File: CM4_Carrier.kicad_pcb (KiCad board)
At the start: 4 copper layers, 47 x 88.8 mm, 102 parts, among them J1 Conn_01x22_Female, J10 Conn_01x20, J12 10018783-11200TLF, J13 BM04B-GHS-TBT(LF)(SN)(N), J14 BM04B-GHS-TBT(LF)(SN)(N), J15 Conn_01x22_Female, J16 XT30, J17 Molex 470531000, J18 BM04B-GHS-TBT(LF)(SN)(N), J2 Conn_01x22_Female, J21 BM04B-GHS-TBT(LF)(SN)(N), J3 USB4085-GF-A_REVA, J4 2199119-4, J6 THD-02-R, J7 Micro_SD_Card_Det, J8 HDMI_D_1.4, J9 Conn_02x08_Odd_Even, Q1 DMP3013SFV-7, SW1 SW_SPST, U1 TPD4EUSB30, U10 AP22653W6, U11 EMC2301-1-ACZL-TR, U12 RT9742SNGV, U13 FSUSB42MUX, U18 RT9742GGJ5, U2 TPD4EUSB30, U3 LMR33640DDDAR, U4 TPD4EUSB30, U6 USB2514B-I/M2, U7 AP22653W6, U9 74LVC1G07SE-7, Y1 ECS-240-18-33-JGN-TR

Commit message: lots of changes, added usb power connections, gpio, hdmi, etc
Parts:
- removed J12: 10018783-11200TLF, CM4IO:PCIex1-36
- removed J4: 2199119-4, Open-HD:TE_2199119-4
- removed J6: THD-02-R, Connector_PinHeader_2.54mm:PinHeader_2x02_P2.54mm_Vertical
- removed R5: 0R, Resistor_SMD:R_0805_2012Metric_Pad1.15x1.40mm_HandSolder
- added TP1: TestPoint, Connector_PinHeader_2.00mm:PinHeader_1x01_P2.00mm_Vertical, F.Cu at (175.1, 80.8)
- R2, R3: moved to F.Cu
- R6, R7: moved to B.Cu
- moved R7 168.1 mm to (128.7, 88.5), turned to -90 degrees
- moved R6 165.6 mm to (126.1, 87.0), turned to 90 degrees
- moved U1 15.0 mm to (153.9, 101.9), turned to 90 degrees
- moved D1 13.7 mm to (94.0, 115.3)
- moved D2 13.7 mm to (85.2, 115.3)
- moved R1 13.7 mm to (88.2, 115.3)
- moved R10 13.7 mm to (97.0, 115.3)
- moved R36 12.5 mm to (115.5, 130.4), turned to 90 degrees
- moved R2 6.12 mm to (153.4, 101.0), turned to -90 degrees
- moved R3 4.81 mm to (154.4, 101.0), turned to -90 degrees
- moved R11 3.20 mm to (143.3, 126.9)
- moved C1 3.05 mm to (140.2, 96.8)
- moved C2 2.33 mm to (119.9, 127.7), turned to 0 degrees
- moved R18 1.94 mm to (143.2, 107.9)
- moved C11 1.78 mm to (132.2, 124.0)
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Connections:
- J1 pad 20: /CM4_HighSpeed/SCL1 -> /ID_SC
- J1 pad 21: /CM4_HighSpeed/SDA1 -> /ID_SD
- J15 pad 20: /CM4_HighSpeed/SCL1 -> /ID_SC
- J15 pad 21: /CM4_HighSpeed/SDA1 -> /ID_SD
- J3 pad P1: GND -> Net-(J3-PadP1)
- J3 pad P2: GND -> Net-(J3-PadP1)
- J3 pad P3: GND -> Net-(J3-PadP1)
- J3 pad P4: GND -> Net-(J3-PadP1)
- Module1 pad 102: /PCIE_CLK_nREQ -> /CM4_HighSpeed/PCIE_CLK_nREQ
- Module1 pad 109: /PCIE_nRST -> /CM4_HighSpeed/PCIE_nRST
- Module1 pad 110: /PCIE_CLK_P -> /CM4_HighSpeed/PCIE_CLK_P
- Module1 pad 112: /PCIE_CLK_N -> /CM4_HighSpeed/PCIE_CLK_N
- Module1 pad 116: /PCIE_RX_P -> /CM4_HighSpeed/PCIE_RX_P
- Module1 pad 118: /PCIE_RX_N -> /CM4_HighSpeed/PCIE_RX_N
- Module1 pad 122: /PCIE_TX_P -> /CM4_HighSpeed/PCIE_TX_P
- Module1 pad 124: /PCIE_TX_N -> /CM4_HighSpeed/PCIE_TX_N
- Module1 pad 78: /GPIO_VREF -> /+3.3v
- R6 pad 1: /GPIO_VREF -> /+3.3v
- R6 pad 2: /CM4_HighSpeed/SDA1 -> /ID_SD
- R7 pad 1: /GPIO_VREF -> /+3.3v
- R7 pad 2: /CM4_HighSpeed/SCL1 -> /ID_SC
- U2 pad 1: /CM4_GPIO ( Ethernet, GPIO, SDCARD)/TRD1_P -> /CM4_GPIO ( Ethernet, GPIO, SDCARD)/TRD0_N
- U2 pad 10: /CM4_GPIO ( Ethernet, GPIO, SDCARD)/TRD1_P -> /CM4_GPIO ( Ethernet, GPIO, SDCARD)/TRD0_N
- U2 pad 2: /CM4_GPIO ( Ethernet, GPIO, SDCARD)/TRD1_N -> /CM4_GPIO ( Ethernet, GPIO, SDCARD)/TRD0_P
- U2 pad 4: /CM4_GPIO ( Ethernet, GPIO, SDCARD)/TRD0_N -> /CM4_GPIO ( Ethernet, GPIO, SDCARD)/TRD1_P
- U2 pad 5: /CM4_GPIO ( Ethernet, GPIO, SDCARD)/TRD0_P -> /CM4_GPIO ( Ethernet, GPIO, SDCARD)/TRD1_N
- U2 pad 6: /CM4_GPIO ( Ethernet, GPIO, SDCARD)/TRD0_P -> /CM4_GPIO ( Ethernet, GPIO, SDCARD)/TRD1_N
- U2 pad 7: /CM4_GPIO ( Ethernet, GPIO, SDCARD)/TRD0_N -> /CM4_GPIO ( Ethernet, GPIO, SDCARD)/TRD1_P
- U2 pad 9: /CM4_GPIO ( Ethernet, GPIO, SDCARD)/TRD1_N -> /CM4_GPIO ( Ethernet, GPIO, SDCARD)/TRD0_P
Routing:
- net /CM4_HighSpeed/CAM1_D2_P: track 0.00 -> 58.0 mm, vias 0 -> 1
- net /CM4_HighSpeed/CAM1_C_P: track 0.00 -> 57.4 mm, vias 0 -> 1
- net /CM4_HighSpeed/CAM1_D2_N: track 0.00 -> 57.4 mm, vias 0 -> 1
- net /CM4_HighSpeed/CAM1_C_N: track 0.00 -> 56.8 mm, vias 0 -> 1
- net /CM4_HighSpeed/CAM1_D1_P: track 0.00 -> 56.7 mm, vias 0 -> 1
- net /CM4_HighSpeed/CAM1_D1_N: track 0.00 -> 56.1 mm, vias 0 -> 1
- net /CM4_HighSpeed/CAM1_D0_P: track 0.00 -> 56.1 mm, vias 0 -> 1
- net /CM4_HighSpeed/CAM1_D0_N: track 0.00 -> 55.4 mm, vias 0 -> 1
- net /CM4_HighSpeed/CAM0_D1_P: track 0.00 -> 48.3 mm, vias 0 -> 1
- net /CM4_HighSpeed/CAM0_D1_N: track 0.00 -> 47.7 mm, vias 0 -> 1
- net /CM4_HighSpeed/CAM0_D0_P: track 0.00 -> 46.6 mm, vias 0 -> 1
- net /CM4_HighSpeed/CAM0_C_P: track 3.21 -> 49.7 mm, vias 0 -> 1
- net /CM4_HighSpeed/CAM0_C_N: track 2.76 -> 49.1 mm, vias 0 -> 1
- net /CM4_HighSpeed/CAM0_D0_N: track 0.00 -> 46.0 mm, vias 0 -> 1
- net /CM4_GPIO ( Ethernet, GPIO, SDCARD)/GPIO2: track 0.00 -> 42.7 mm, vias 0 -> 2
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- added copper zone on In2.Cu, net /USB2-HUB/VBUS_HP
- added copper zone on F.Cu, net /USB2-HUB/VBUS_LP
- added copper zone on F.Cu, net GND
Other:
- board text removed: "DISP0"
- board text removed: "DISP1"
- board text removed: "Fit jumper to disable eMMC Boot"
- board text removed: "Fit jumper to disable writing to EEPROM"
- board text removed: "Fit two jumpers For CAM0 and DISP0"
- board text removed: "HDMI0"
- board text removed: "PCIe x1"
- board text removed: "POE"
- board text removed: "RUN GLOBAL_EN"
- board text removed: "Raspberry Pi HAT"
- board text removed: "USB Slave"

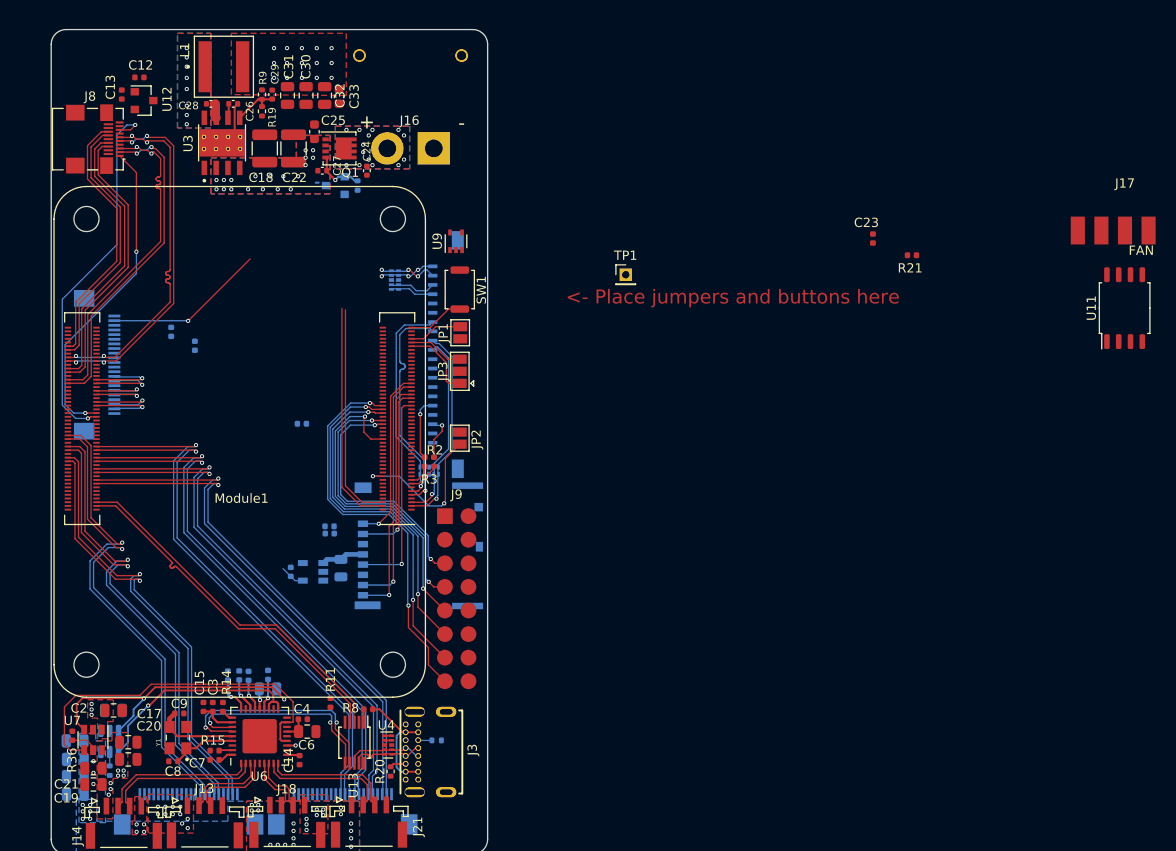
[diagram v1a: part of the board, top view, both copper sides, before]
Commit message: will probably have to rip up CSI connections, going to try lane swapping and reducing number of lanes
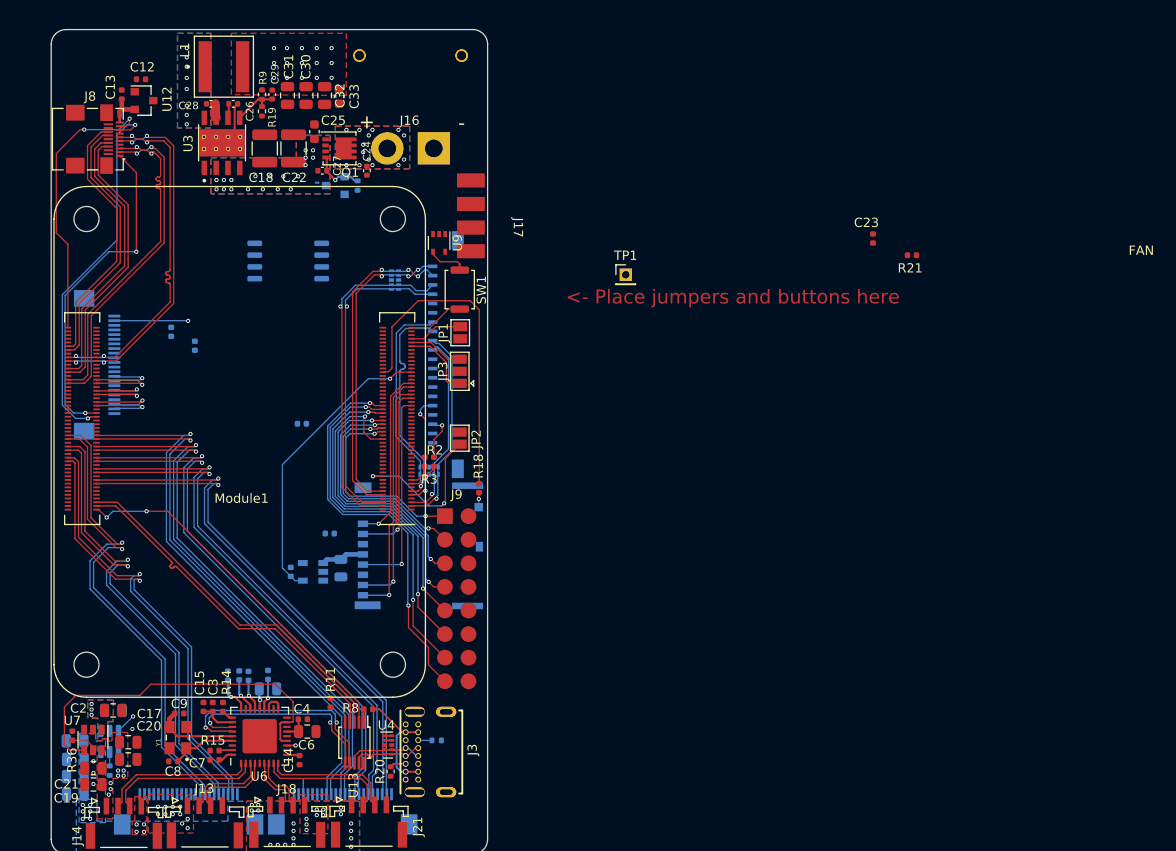
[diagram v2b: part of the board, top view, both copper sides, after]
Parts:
- R18: moved to F.Cu
- U11: moved to B.Cu
- moved U11 90.2 mm to (138.7, 79.3), turned to 0 degrees
- moved J17 65.4 mm to (160.9, 73.2), turned to -90 degrees
- moved R18 16.6 mm to (159.3, 103.8), turned to -90 degrees
- moved U9 1.83 mm to (155.0, 77.4), turned to -90 degrees
- moved C12 0.27 mm to (122.9, 59.8)
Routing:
- net /CM4_HighSpeed/CAM1_D3_P: track 0.00 -> 58.9 mm, vias 0 -> 1
- net /CM4_HighSpeed/CAM1_D3_N: track 0.00 -> 58.3 mm, vias 0 -> 1
- net /USBOTG: track 1.53 -> 41.1 mm, vias 0 -> 2
- net /CM4_GPIO ( Ethernet, GPIO, SDCARD)/SD_DET: track 0.00 -> 35.3 mm
- net /CM4_HighSpeed/HDMI0_SCL: track 0.00 -> 30.4 mm, vias 0 -> 2
- net /CM4_GPIO ( Ethernet, GPIO, SDCARD)/SD_PWR_ON: track 2.66 -> 31.9 mm, vias 0 -> 1
- net /USB2-HUB/PWR1: track 32.3 -> 3.15 mm, vias 3 -> 2
- net /CM4_GPIO ( Ethernet, GPIO, SDCARD)/TRD0_N: track 6.57 -> 34.9 mm
- net /CM4_GPIO ( Ethernet, GPIO, SDCARD)/TRD0_P: track 6.18 -> 33.3 mm
- net /CM4_GPIO ( Ethernet, GPIO, SDCARD)/GPIO22: track 0.00 -> 23.8 mm, vias 0 -> 2
- net /CM4_GPIO ( Ethernet, GPIO, SDCARD)/GPIO10: track 0.00 -> 21.8 mm, vias 0 -> 2
- net /USB2-HUB/nOCS2: track 23.7 -> 2.26 mm
- net /ID_SD: track 17.4 -> 7.96 mm
- net /CM4_GPIO ( Ethernet, GPIO, SDCARD)/TRD1_P: track 29.6 -> 36.6 mm, vias 0 -> 1
- net /CM4_GPIO ( Ethernet, GPIO, SDCARD)/TRD1_N: track 28.6 -> 35.1 mm, vias 0 -> 1
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- added copper zone on B.Cu, net /+5v

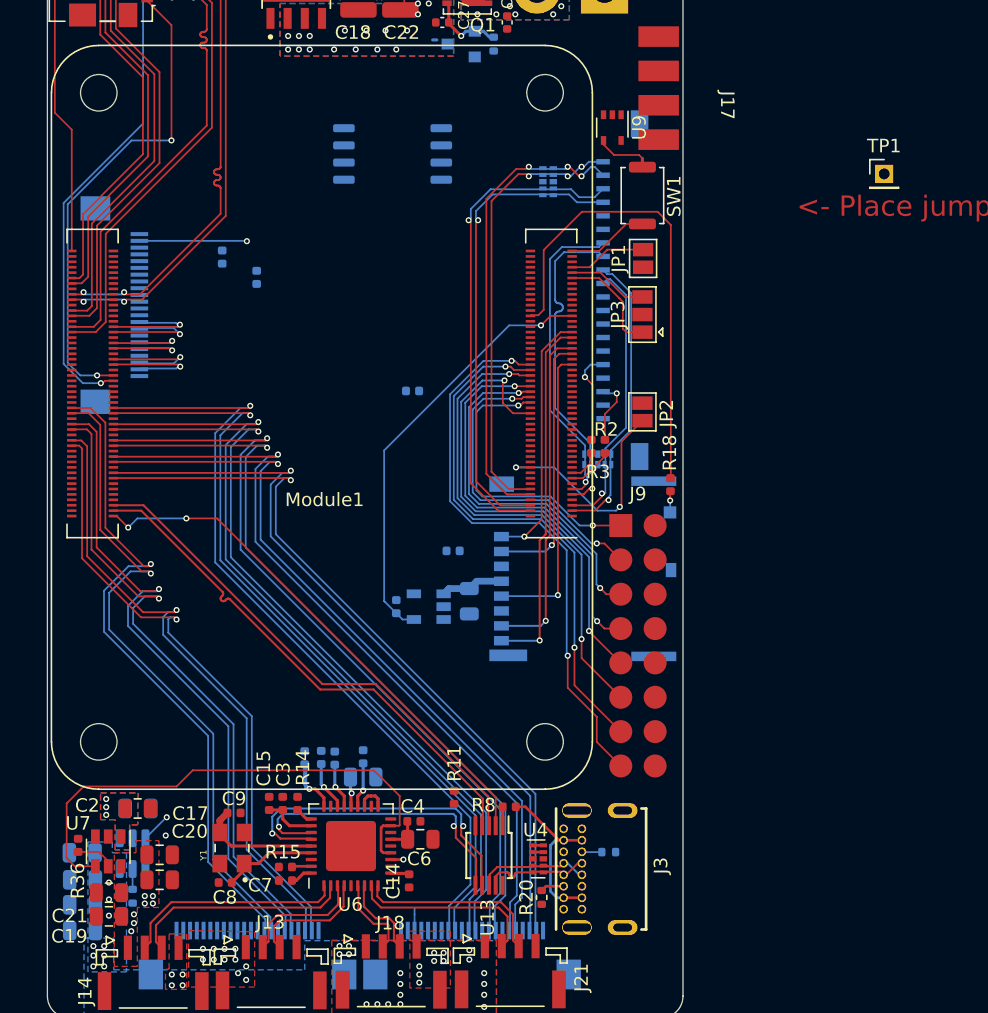
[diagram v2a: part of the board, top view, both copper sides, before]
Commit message: ripped up csi connections
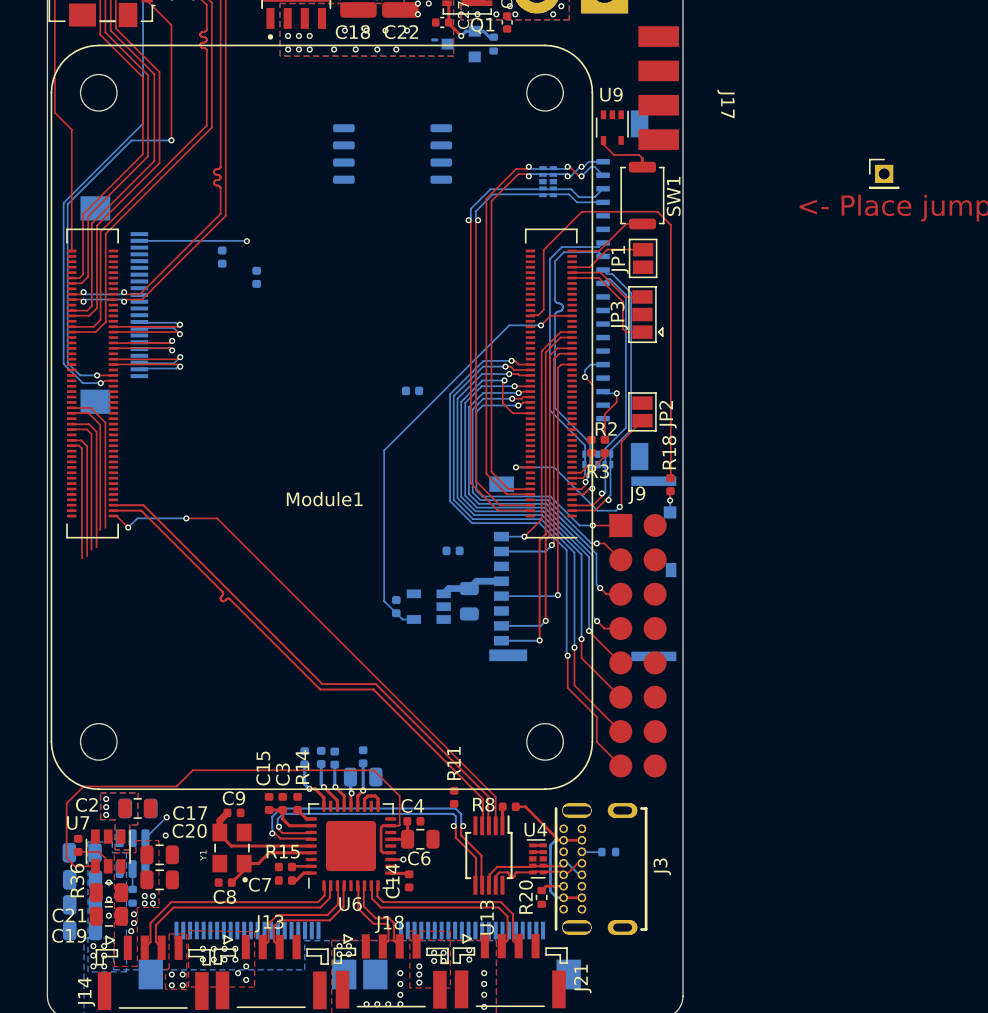
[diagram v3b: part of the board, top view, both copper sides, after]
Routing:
- net /CM4_HighSpeed/CAM1_D3_P: track 58.9 -> 0.10 mm, vias 1 -> 0
- net /CM4_HighSpeed/CAM1_D3_N: track 58.3 -> 0.10 mm, vias 1 -> 0
- net /CM4_HighSpeed/CAM1_D2_P: track 58.0 -> 0.10 mm, vias 1 -> 0
- net /CM4_HighSpeed/CAM1_C_P: track 57.4 -> 0.10 mm, vias 1 -> 0
- net /CM4_HighSpeed/CAM1_D2_N: track 57.4 -> 0.10 mm, vias 1 -> 0
- net /CM4_HighSpeed/CAM1_C_N: track 56.8 -> 0.10 mm, vias 1 -> 0
- net /CM4_HighSpeed/CAM1_D1_P: track 56.7 -> 0.10 mm, vias 1 -> 0
- net /CM4_HighSpeed/CAM1_D1_N: track 56.1 -> 0.10 mm, vias 1 -> 0
- net /CM4_HighSpeed/CAM1_D0_P: track 56.1 -> 0.10 mm, vias 1 -> 0
- net /CM4_HighSpeed/CAM1_D0_N: track 55.4 -> 0.10 mm, vias 1 -> 0
- net /CM4_HighSpeed/CAM0_C_P: track 49.7 -> 10.8 mm, vias 1 -> 0
- net /CM4_HighSpeed/CAM0_C_N: track 49.1 -> 10.3 mm, vias 1 -> 0
- net /CM4_HighSpeed/CAM0_D1_P: track 48.3 -> 10.7 mm, vias 1 -> 0
- net /CM4_HighSpeed/CAM0_D1_N: track 47.7 -> 10.2 mm, vias 1 -> 0
- net /CM4_HighSpeed/CAM0_D0_P: track 46.6 -> 9.53 mm, vias 1 -> 0
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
